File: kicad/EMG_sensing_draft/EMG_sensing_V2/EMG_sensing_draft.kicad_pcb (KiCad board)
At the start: 2 copper layers, 49.4 x 60.1 mm, 157 parts, among them J1 USB_A_0480370001, J2 Conn_01x09, J3 DEBUG, U1 MCP6N11-002E/SN, U10 RP2040, U11 RN4871-I/RM140, U12 MCP1702T-3302E_CB, U13 Opamp_MCP6024T-E/ST, U14 Opamp_MCP6024T-E/ST, U15 Opamp_MCP6024T-E/ST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

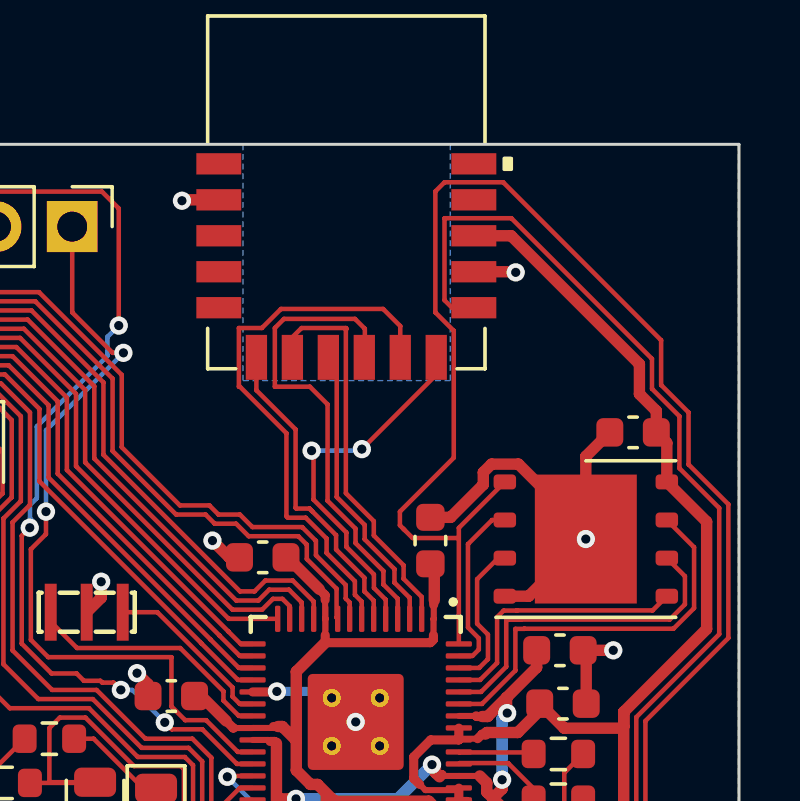
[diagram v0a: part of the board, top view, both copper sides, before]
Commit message: fixed copper fill
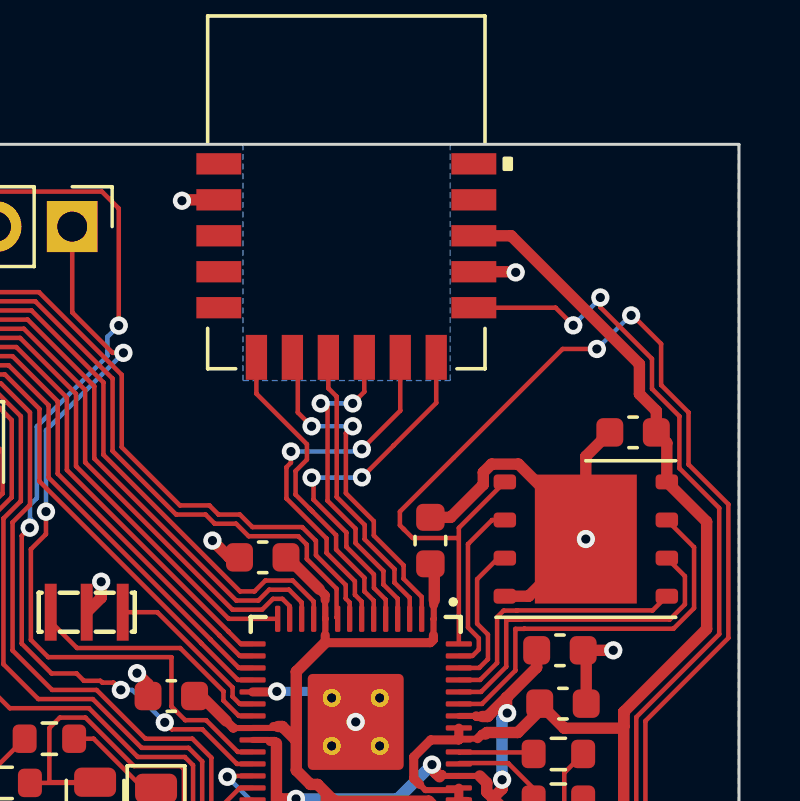
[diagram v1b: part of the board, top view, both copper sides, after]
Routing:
- net Net-(R2-Pad1): track 71.6 -> 61.7 mm, vias 0 -> 2
- net /RST_N: track 18.7 -> 12.7 mm, vias 0 -> 2
- net /RTS: track 16.3 -> 11.1 mm, vias 0 -> 2
- net Net-(R13-Pad1): track 67.7 -> 62.7 mm, vias 0 -> 2
- net /BLE_RX: track 13.3 -> 11.5 mm, vias 0 -> 2
